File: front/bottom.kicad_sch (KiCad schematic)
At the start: 1 part, among them U3 TCA9548APWR

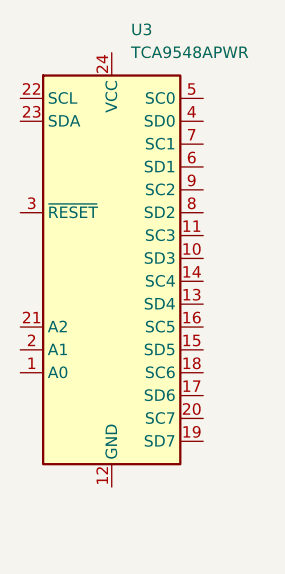
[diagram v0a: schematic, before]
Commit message: add some traces
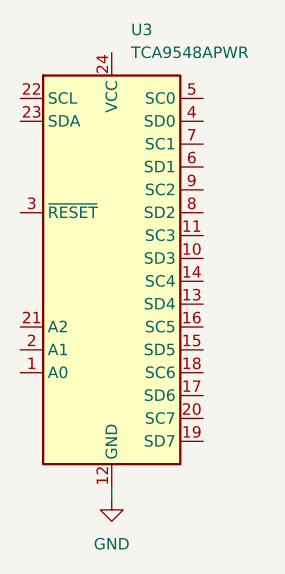
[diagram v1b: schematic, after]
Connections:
- net GND: now reaches U3.12 (GND)
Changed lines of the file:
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@@
 	(generator_version "9.0")
 	(paper "A4")
+	(wire
+		(pts
+			(xy 128.27 121.92) (xy 128.27 120.65)
+		)
+		(stroke
+			(width 0)
+			(type default)
+		)
+	)
 	(symbol
 		(lib_id "Interface_Expansion:TCA9548APWR")
@@
 					(unit 1)
 				)
+			)
+		)
+	)
+	(symbol
+		(lib_id "power:GND")
+		(at 128.27 121.92 0)
+		(unit 1)
+		(exclude_from_sim no)
+		(in_bom yes)
+		(on_board yes)
+		(dnp no)
+		(fields_autoplaced yes)
+		(property "Reference" "#PWR03"
+			(at 128.27 128.27 0)
+			(effects
+				(font
+					(size 1.27 1.27)
+				)
+				(hide yes)
+			)
+		)
+		(property "Value" "GND"
+			(at 128.27 127 0)
+			(effects
+				(font
+					(size 1.27 1.27)
+				)
+			)
+		)
+		(property "Footprint" ""
+			(at 128.27 121.92 0)
+			(effects
+				(font
+					(size 1.27 1.27)
+				)
+				(hide yes)
+			)
+		)
+		(property "Datasheet" ""
+			(at 128.27 121.92 0)
+			(effects
+				(font
+					(size 1.27 1.27)
+				)
+				(hide yes)
+			)
+		)
+		(property "Description" "Power symbol creates a global label with name \"GND\" , ground"
+			(at 128.27 121.92 0)
+			(effects
+				(font
+					(size 1.27 1.27)
+				)
+				(hide yes)
+			)
+		)
+		(pin "1"
+		)
+		(instances
+			(project ""
+				(path "/508f986b-6f1b-4c39-bd57-bae69573a4e7/f87f006e-e62f-4570-8606-fdae847a413a"
+					(reference "#PWR03")
+					(unit 1)
+				)
